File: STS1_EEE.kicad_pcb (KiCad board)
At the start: 4 copper layers, 81.1 x 85 mm, 50 parts, among them J1 Conn_02x20_Odd_Even, J2 Conn_02x20_Odd_Even, SW1 SW_SPST, U1 coordinate_system, U2 ST_Logo, U3 MP28167GQ, U4 MCP1725-3302E_MC, U5 1047

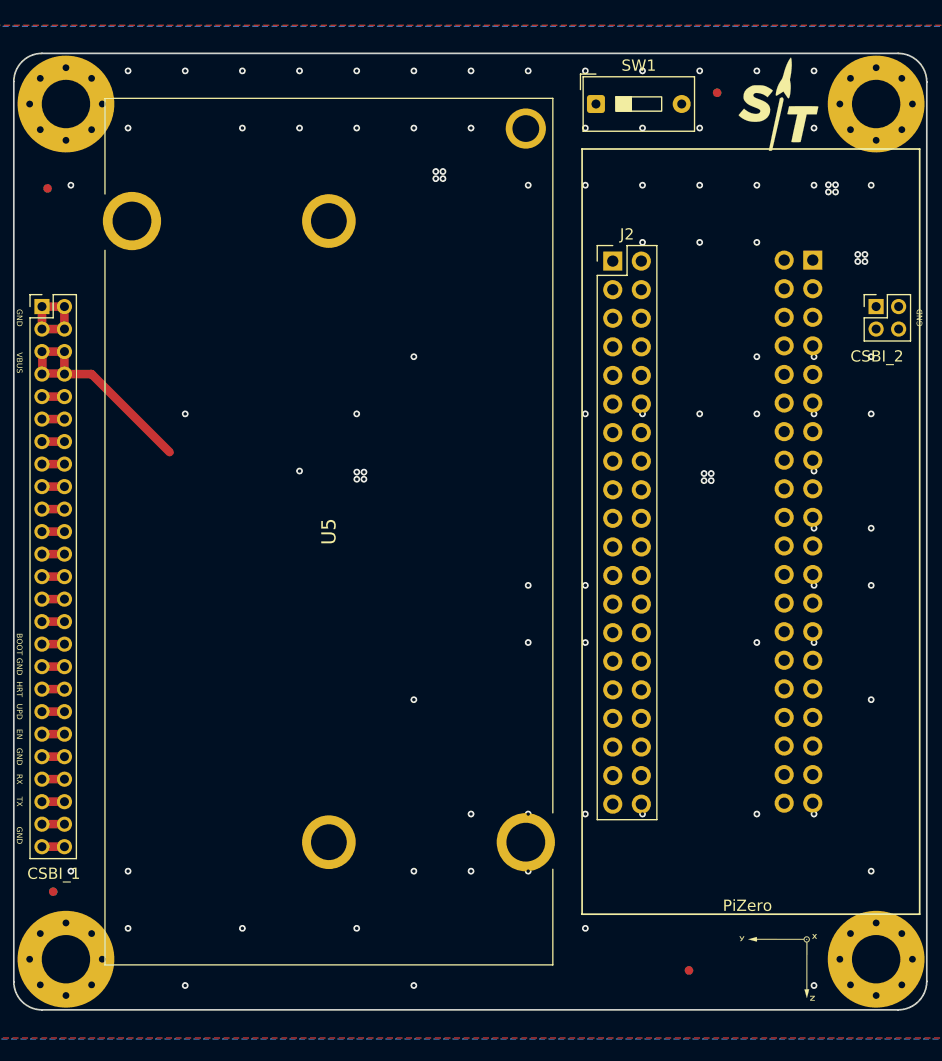
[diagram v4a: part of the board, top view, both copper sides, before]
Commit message: Fix the labels on PiHAT connector
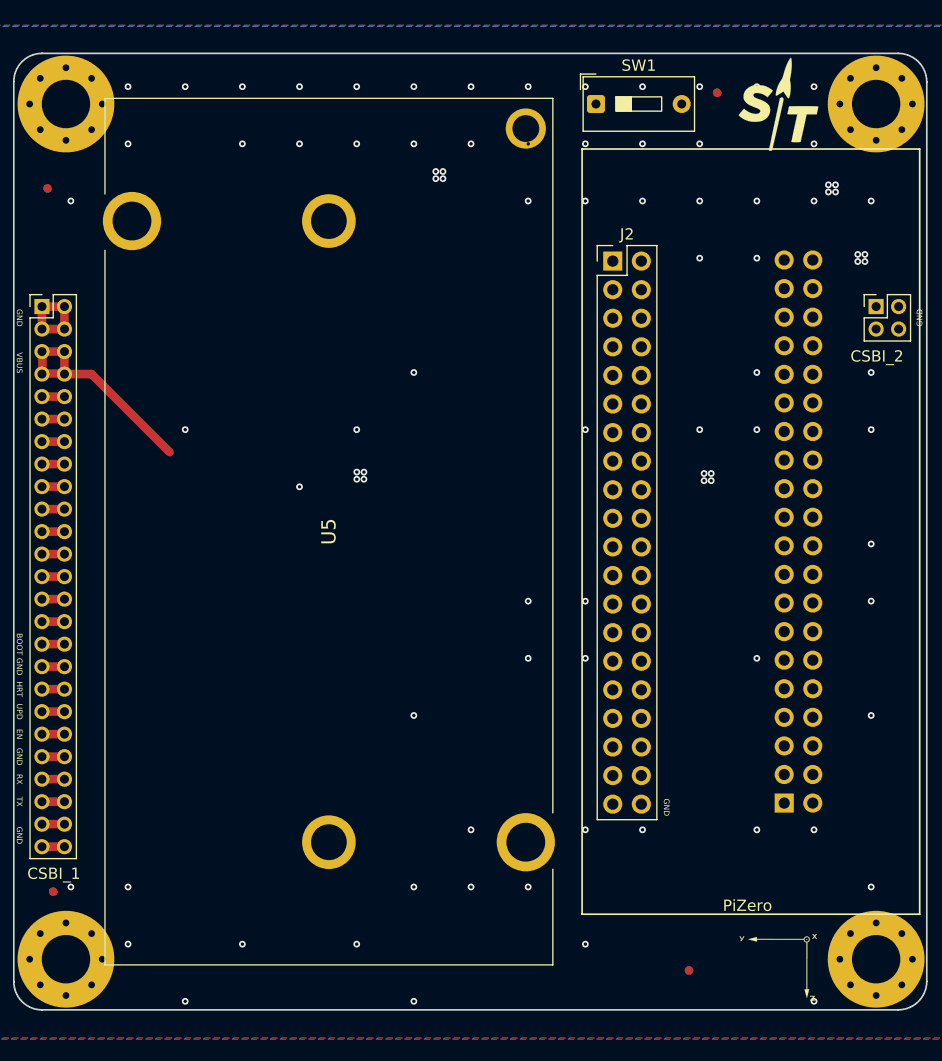
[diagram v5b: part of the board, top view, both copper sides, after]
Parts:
- moved J1 48.3 mm to (184.5, 108.4), turned to 0 degrees
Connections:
- J1 pad 1: unconnected-(J1-Pin_1-Pad1) -> Pi_3V3
- J1 pad 10: GND -> unconnected-(J1-Pin_10-Pad10)
- J1 pad 11: unconnected-(J1-Pin_11-Pad11) -> GPIO17
- J1 pad 12: GPIO17 -> unconnected-(J1-Pin_12-Pad12)
- J1 pad 13: GND -> GPIO27
- J1 pad 14: GPIO27 -> GND
- J1 pad 15: unconnected-(J1-Pin_15-Pad15) -> GPIO22
- J1 pad 16: GPIO22 -> unconnected-(J1-Pin_16-Pad16)
- J1 pad 19: GND -> unconnected-(J1-Pin_19-Pad19)
- J1 pad 2: Pi_3V3 -> unconnected-(J1-Pin_2-Pad2)
- J1 pad 20: unconnected-(J1-Pin_20-Pad20) -> GND
- J1 pad 25: unconnected-(J1-Pin_25-Pad25) -> GND
- J1 pad 26: GND -> unconnected-(J1-Pin_26-Pad26)
- J1 pad 29: GND -> unconnected-(J1-Pin_29-Pad29)
- J1 pad 3: unconnected-(J1-Pin_3-Pad3) -> SDA0
- J1 pad 30: unconnected-(J1-Pin_30-Pad30) -> GND
- J1 pad 33: GND -> unconnected-(J1-Pin_33-Pad33)
- J1 pad 34: unconnected-(J1-Pin_34-Pad34) -> GND
- J1 pad 39: unconnected-(J1-Pin_39-Pad39) -> GND
- J1 pad 4: SDA0 -> unconnected-(J1-Pin_4-Pad4)
- J1 pad 40: GND -> unconnected-(J1-Pin_40-Pad40)
- J1 pad 5: GND -> SCL0
- J1 pad 6: SCL0 -> GND
- J1 pad 9: unconnected-(J1-Pin_9-Pad9) -> GND
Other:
- board text added: "3V3"
- board text added: "IO17"
- board text added: "IO22"
- board text added: "IO27"
- board text added: "SCL"
- board text added: "SDA"

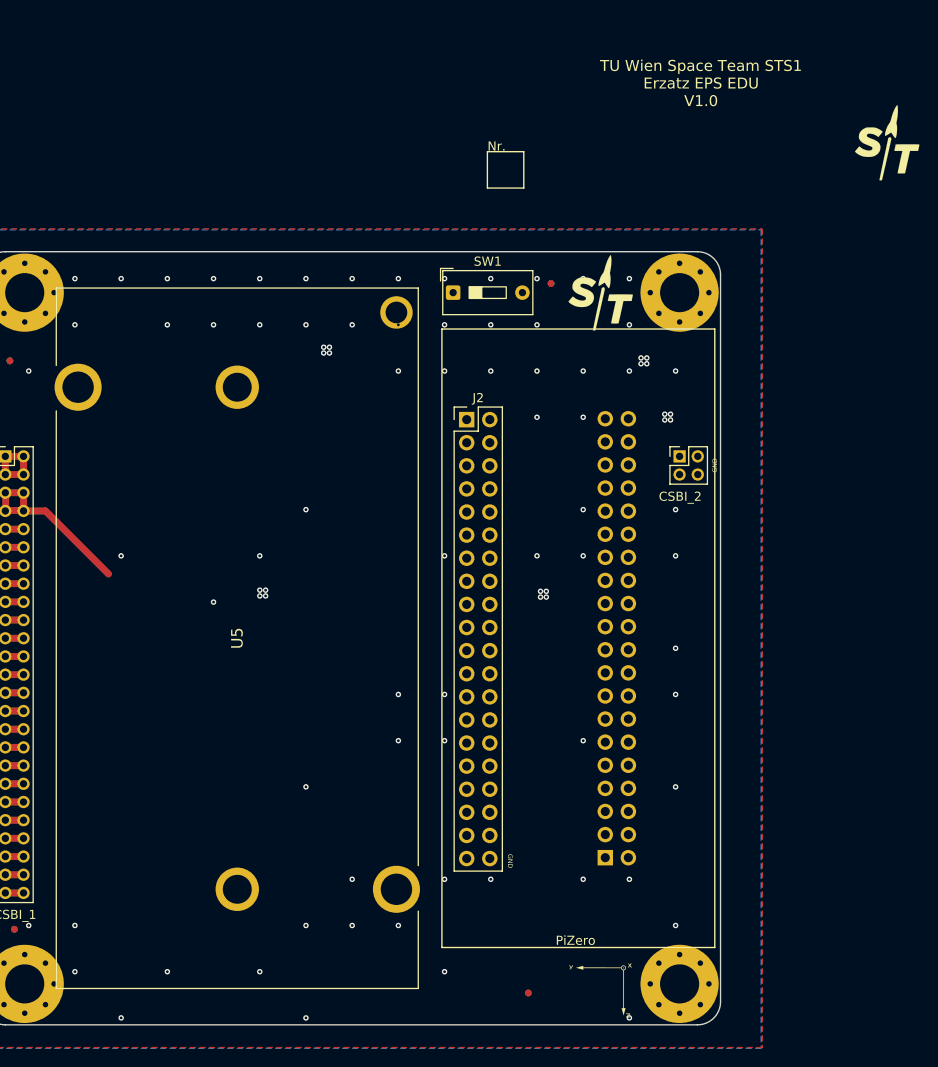
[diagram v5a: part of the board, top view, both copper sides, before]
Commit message: Replace 1047 battery holder with 1048P (battery contacts connect to PCB using pads)
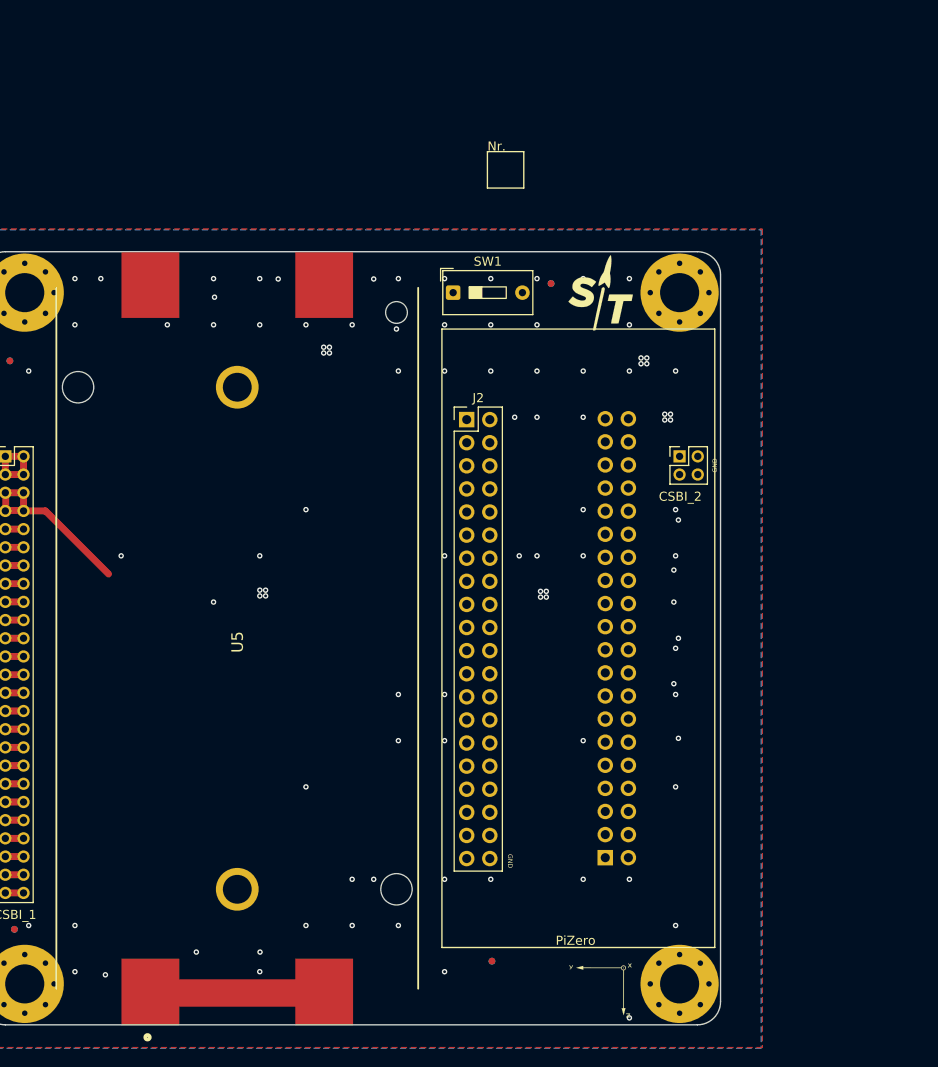
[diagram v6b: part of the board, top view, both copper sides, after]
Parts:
- U2: moved to B.Cu
- U5: footprint STS_EEE:1047 -> STS_EEE:1048P
- moved U2 108.8 mm to (157.5, 121.8), turned to 180 degrees
- moved FID1 5.32 mm to (172.0, 119.8)
- moved FID8 5.32 mm to (172.0, 119.8)
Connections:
- U5 pad 1: unconnected-(U5-Pad1) -> Net-(U5-Pad1)
- U5 pad 2: unconnected-(U5-Pad2) -> Net-(U5-Pad1)

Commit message: Finilize connection and placement of components
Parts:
- removed C13: 4.7u, Capacitor_SMD:C_0603_1608Metric
- removed D23: PTVS3V3S1UR,115, Diode_SMD:D_SOD-123
- removed the D3 at (50.9, 47.8)
- removed the R3 at (50.7, 50.6)
- removed the U4 at (75.0, 101.1)
- moved TP1 154.0 mm to (191.0, 45.2)
- moved TP2 154.0 mm to (194.1, 45.2)
- moved D3 120.7 mm to (184.4, 46.0), turned to 90 degrees
- moved R3 118.2 mm to (186.2, 46.0), turned to 90 degrees
- moved D4 116.4 mm to (180.0, 46.0), turned to 90 degrees
- moved R4 113.8 mm to (181.8, 46.0), turned to 90 degrees
- moved C1 89.0 mm to (141.5, 94.1), turned to -90 degrees
- moved R2 88.2 mm to (135.7, 97.2), turned to 180 degrees
- moved D1 87.9 mm to (145.2, 90.1), turned to -90 degrees
- moved C6 84.8 mm to (135.1, 94.9), turned to -90 degrees
- moved R1 84.4 mm to (144.1, 87.8), turned to 90 degrees
- moved C5 83.4 mm to (133.2, 94.8), turned to -90 degrees
- moved C3 83.3 mm to (138.3, 91.4), turned to -90 degrees
- moved C2 81.9 mm to (140.8, 88.3), turned to 0 degrees
- moved C4 81.6 mm to (144.0, 85.2), turned to 180 degrees
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- renumbered D4 to D3, D5 to D4, R4 to R3, R5 to R4, U5 to U4
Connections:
- CSBI_1 pad 43: UART_COBC_EDU_2 -> Pi_TX
- CSBI_1 pad 44: UART_COBC_EDU_2 -> Pi_TX
- CSBI_1 pad 45: UART_COBC_EDU_1 -> Pi_RX
- CSBI_1 pad 46: UART_COBC_EDU_1 -> Pi_RX
- J2 pad 7: TX -> Pi_TX
- J2 pad 9: RX -> Pi_RX
- R3 pad 1: 3V3 -> Pi_3V3
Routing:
- net Pi_3V3: track 0.00 -> 97.4 mm, vias 0 -> 1
- net VBUS: track 34.3 -> 120.3 mm
- net Pi_RX: track 0.00 -> 72.1 mm
- net Pi_TX: track 0.00 -> 72.0 mm
- net VBAT: track 27.8 -> 68.6 mm
- net GPIO17: track 0.00 -> 28.7 mm, vias 0 -> 1
- net GPIO27: track 0.00 -> 23.0 mm, vias 0 -> 2
- net EDU_EN: track 2.99 -> 23.0 mm
- net GPIO22: track 0.00 -> 17.9 mm
- net Net-(SW1-A): track 0.00 -> 14.5 mm
- net UART_COBC_EDU_2: track 2.00 -> 0.00 mm
- net UART_COBC_EDU_1: track 2.00 -> 0.00 mm
- net Net-(D4-A): track 0.00 -> 1.82 mm
- net Net-(D3-A): track 0.00 -> 1.82 mm
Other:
- board text added: "5V"

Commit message: Fix DRC errors
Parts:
- removed TP1, TP2: TestPoint, TestPoint:TestPoint_Pad_1.0x1.0mm
- moved D1 1.17 mm to (146.0, 89.3), turned to 180 degrees
- moved C1 0.51 mm to (142.0, 94.1)
- moved C3 0.23 mm to (138.5, 91.4)
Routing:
- net GND: vias 100 -> 103
